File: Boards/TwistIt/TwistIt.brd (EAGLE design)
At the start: 39.9 x 54.8 mm, 19 parts

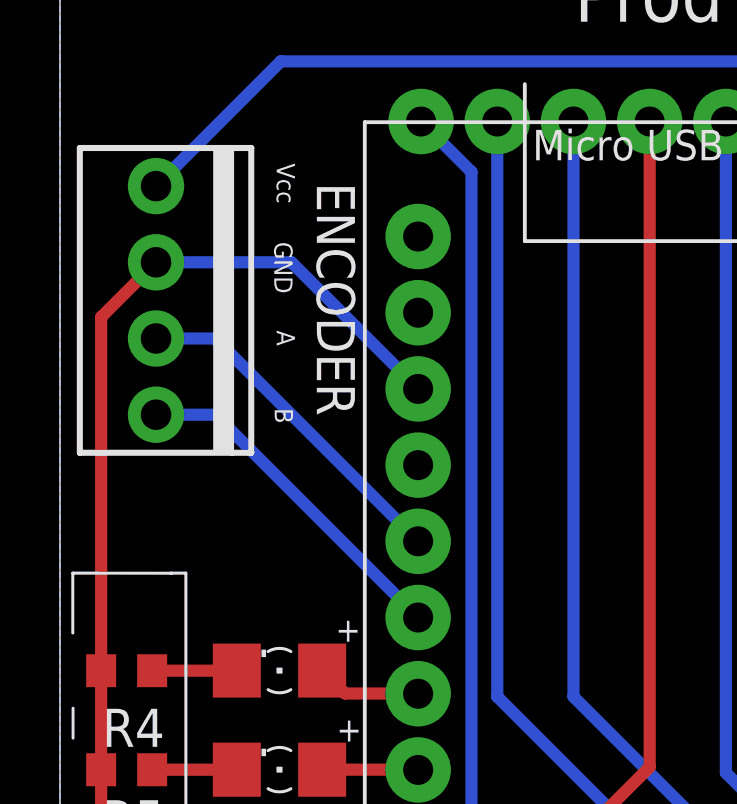
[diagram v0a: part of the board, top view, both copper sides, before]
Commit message: Add pullup resistors to encoders
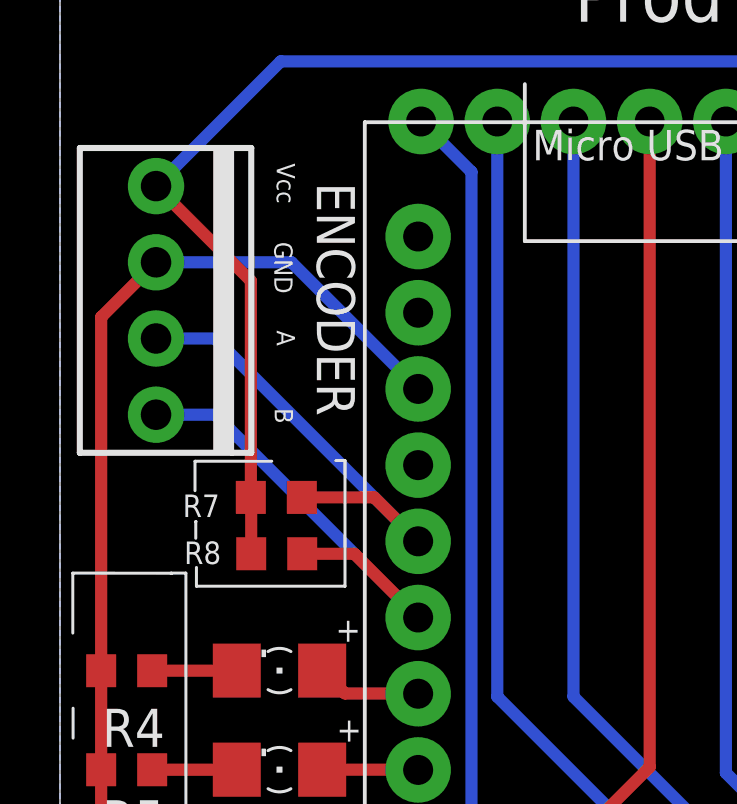
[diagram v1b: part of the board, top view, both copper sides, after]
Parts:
- added R7, R8: 10k, pie:R0603
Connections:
- net A: now also R7.1
- net B: now also R8.1
- net VCC: now also R7.2, R8.2
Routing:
- net VCC: track 74.1 -> 87.6 mm
- net B: track 11.5 -> 16.3 mm
- net A: track 11.5 -> 16.0 mm
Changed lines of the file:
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@@
 <layer number="22" name="bPlace" color="24" fill="1" visible="yes" active="yes"/>
 <layer number="23" name="tOrigins" color="15" fill="1" visible="yes" active="yes"/>
-<layer number="24" name="bOrigins" color="15" fill="1" visible="yes" active="yes"/>
+<layer number="24" name="bOrigins" color="15" fill="1" visible="no" active="yes"/>
 <layer number="25" name="tNames" color="7" fill="1" visible="yes" active="yes"/>
-<layer number="26" name="bNames" color="7" fill="1" visible="yes" active="yes"/>
+<layer number="26" name="bNames" color="7" fill="1" visible="no" active="yes"/>
 <layer number="27" name="tValues" color="7" fill="1" visible="yes" active="yes"/>
-<layer number="28" name="bValues" color="7" fill="1" visible="yes" active="yes"/>
+<layer number="28" name="bValues" color="7" fill="1" visible="no" active="yes"/>
 <layer number="29" name="tStop" color="7" fill="3" visible="yes" active="yes"/>
 <layer number="30" name="bStop" color="7" fill="6" visible="yes" active="yes"/>
@@
 <text x="10.058" y="24.313" size="0.8128" layer="25" font="vector" rot="MR0">+</text>
 <text x="10.003" y="20.986" size="0.8128" layer="25" font="vector" rot="MR0">+</text>
+<wire x1="7.059" y1="33.658" x2="4.501" y2="33.658" width="0.1" layer="21"/>
+<wire x1="4.501" y1="33.658" x2="4.501" y2="32.675" width="0.1" layer="21"/>
+<wire x1="4.536" y1="31.645" x2="4.525" y2="31.645" width="0.1" layer="21"/>
+<wire x1="4.525" y1="31.645" x2="4.525" y2="31.089" width="0.1" layer="21"/>
+<wire x1="4.548" y1="30.118" x2="4.548" y2="29.493" width="0.1" layer="21"/>
+<wire x1="4.548" y1="29.493" x2="9.5" y2="29.493" width="0.1" layer="21"/>
+<wire x1="9.5" y1="29.493" x2="9.5" y2="33.681" width="0.1" layer="21"/>
+<wire x1="9.5" y1="33.681" x2="9.188" y2="33.681" width="0.1" layer="21"/>
 </plain>
 <attributes>
@@
 <attribute name="VALUE" x="-1.244" y="44.099" size="1.27" layer="27" font="vector" rot="R270"/>
 </element>
+<element name="R7" library="pie" package="R0603" value="10k" x="7.212" y="32.452" smashed="yes" rot="R180">
+<attribute name="MANUFACTURER_PART_NUMBER" value="" x="7.212" y="32.452" size="1.778" layer="27" rot="R180" display="off"/>
+<attribute name="DISTRIBUTOR" value="DigiKey" x="7.212" y="32.452" size="1.778" layer="27" rot="R180" display="off"/>
+<attribute name="PACKAGE" value="R0603" x="7.212" y="32.452" size="1.778" layer="27" rot="R180" display="off"/>
+<attribute name="NOTES" value="Cut Tape" x="7.212" y="32.452" size="1.778" layer="27" rot="R180" display="off"/>
+<attribute name="DESCRIPTION" value="RESISTOR, American symbol" x="7.212" y="32.452" size="1.778" layer="27" rot="R180" display="off"/>
+<attribute name="MANUFACTURER" value="Rohm Semiconductor" x="7.212" y="32.452" size="1.778" layer="27" rot="R180" display="off"/>
+<attribute name="DISTRIBUTOR_PART_NUMBER" value="" x="7.212" y="32.452" size="1.778" layer="27" rot="R180" display="off"/>
+<attribute name="NAME" x="5.323" y="32.548" size="0.75" layer="25" font="vector" ratio="10" rot="R180"/>
+<attribute name="VALUE" x="9.199" y="34.125" size="0.75" layer="27" font="vector" rot="R180"/>
+</element>
+<element name="R8" library="pie" package="R0603" value="10k" x="7.224" y="30.573" smashed="yes" rot="R180">
+<attribute name="MANUFACTURER_PART_NUMBER" value="" x="7.224" y="30.573" size="1.778" layer="27" rot="R180" display="off"/>
+<attribute name="DISTRIBUTOR" value="DigiKey" x="7.224" y="30.573" size="1.778" layer="27" rot="R180" display="off"/>
+<attribute name="PACKAGE" value="R0603" x="7.224" y="30.573" size="1.778" layer="27" rot="R180" display="off"/>
+<attribute name="NOTES" value="Cut Tape" x="7.224" y="30.573" size="1.778" layer="27" rot="R180" display="off"/>
+<attribute name="DESCRIPTION" value="RESISTOR, American symbol" x="7.224" y="30.573" size="1.778" layer="27" rot="R180" display="off"/>
+<attribute name="MANUFACTURER" value="Rohm Semiconductor" x="7.224" y="30.573" size="1.778" layer="27" rot="R180" display="off"/>
+<attribute name="DISTRIBUTOR_PART_NUMBER" value="" x="7.224" y="30.573" size="1.778" layer="27" rot="R180" display="off"/>
+<attribute name="NAME" x="5.37" y="30.981" size="0.75" layer="25" font="vector" ratio="10" rot="R180"/>
+</element>
 </elements>
 <signals>
@@
 <wire x1="33.016" y1="5.512865625" x2="33.016" y2="33.278" width="0.4064" layer="16"/>
 <wire x1="33.016" y1="33.278" x2="32.766" y2="33.528" width="0.4064" layer="16"/>
+<contactref element="R8" pad="2"/>
+<contactref element="R7" pad="2"/>
+<wire x1="6.374" y1="30.573" x2="6.374" y2="32.44" width="0.4064" layer="1"/>
+<wire x1="6.374" y1="32.44" x2="6.362" y2="32.452" width="0.4064" layer="1"/>
+<wire x1="3.201" y1="42.829" x2="6.362" y2="39.668" width="0.4064" layer="1"/>
+<wire x1="6.362" y1="39.668" x2="6.362" y2="32.452" width="0.4064" layer="1"/>
 </signal>
 <signal name="P1">
@@
 <wire x1="3.201" y1="37.749" x2="5.177" y2="37.749" width="0.4064" layer="16"/>
 <wire x1="5.177" y1="37.749" x2="11.938" y2="30.988" width="0.4064" layer="16"/>
+<contactref element="R7" pad="1"/>
+<wire x1="8.062" y1="32.452" x2="10.474" y2="32.452" width="0.4064" layer="1"/>
+<wire x1="10.474" y1="32.452" x2="11.938" y2="30.988" width="0.4064" layer="1"/>
 </signal>
 <signal name="B">
@@
 <wire x1="3.201" y1="35.209" x2="5.177" y2="35.209" width="0.4064" layer="16"/>
 <wire x1="5.177" y1="35.209" x2="11.938" y2="28.448" width="0.4064" layer="16"/>
+<contactref element="R8" pad="1"/>
+<wire x1="8.074" y1="30.573" x2="9.813" y2="30.573" width="0.4064" layer="1"/>
+<wire x1="9.813" y1="30.573" x2="11.938" y2="28.448" width="0.4064" layer="1"/>
 </signal>
 </signals>

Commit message: Change pullup resistor vcalue
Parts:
- R7, R8: value 10k -> 1k
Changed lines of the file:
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@@
 <attribute name="VALUE" x="-1.244" y="44.099" size="1.27" layer="27" font="vector" rot="R270"/>
 </element>
-<element name="R7" library="pie" package="R0603" value="10k" x="7.212" y="32.452" smashed="yes" rot="R180">
+<element name="R7" library="pie" package="R0603" value="1k" x="7.212" y="32.452" smashed="yes" rot="R180">
 <attribute name="MANUFACTURER_PART_NUMBER" value="" x="7.212" y="32.452" size="1.778" layer="27" rot="R180" display="off"/>
 <attribute name="DISTRIBUTOR" value="DigiKey" x="7.212" y="32.452" size="1.778" layer="27" rot="R180" display="off"/>
@@
 <attribute name="DISTRIBUTOR_PART_NUMBER" value="" x="7.212" y="32.452" size="1.778" layer="27" rot="R180" display="off"/>
 <attribute name="NAME" x="5.323" y="32.548" size="0.75" layer="25" font="vector" ratio="10" rot="R180"/>
-<attribute name="VALUE" x="9.199" y="34.125" size="0.75" layer="27" font="vector" rot="R180"/>
+<attribute name="VALUE" x="8.817" y="34.165" size="0.75" layer="27" font="vector" rot="R180"/>
 </element>
-<element name="R8" library="pie" package="R0603" value="10k" x="7.224" y="30.573" smashed="yes" rot="R180">
+<element name="R8" library="pie" package="R0603" value="1k" x="7.224" y="30.573" smashed="yes" rot="R180">
 <attribute name="MANUFACTURER_PART_NUMBER" value="" x="7.224" y="30.573" size="1.778" layer="27" rot="R180" display="off"/>
 <attribute name="DISTRIBUTOR" value="DigiKey" x="7.224" y="30.573" size="1.778" layer="27" rot="R180" display="off"/>

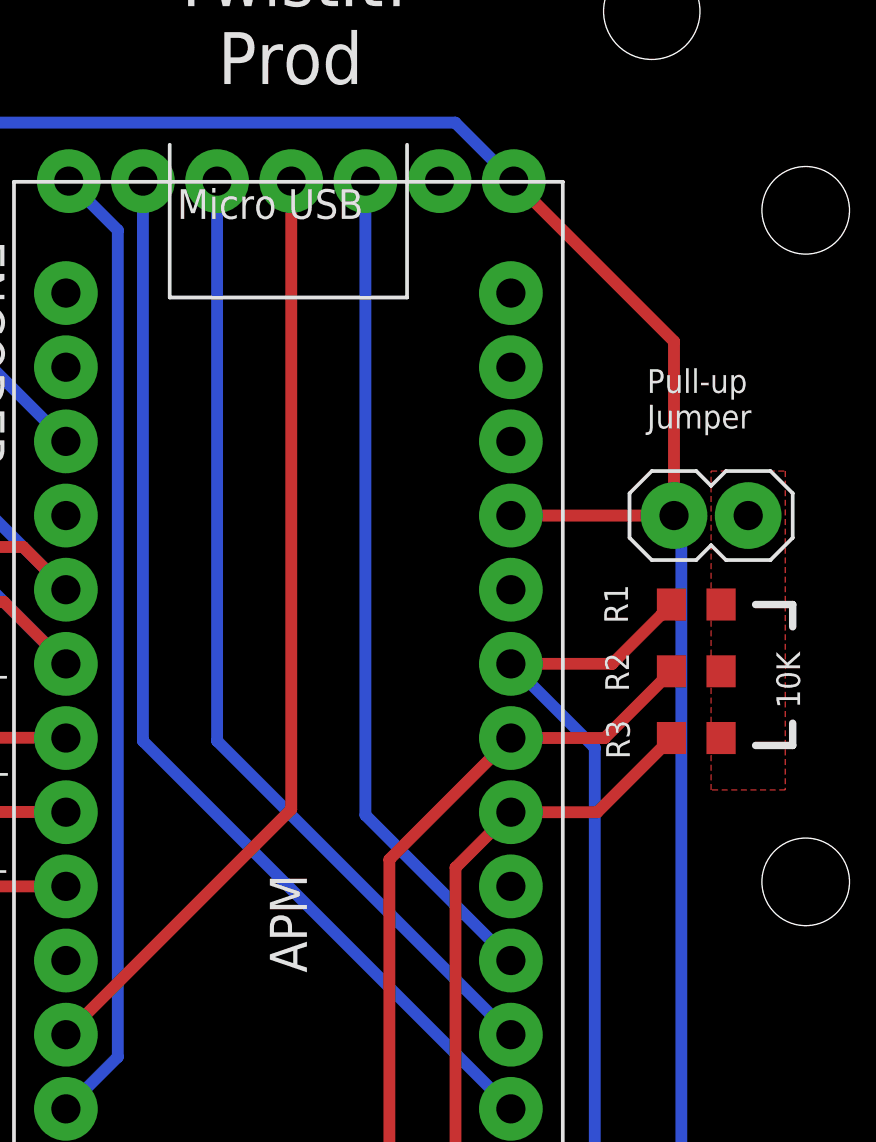
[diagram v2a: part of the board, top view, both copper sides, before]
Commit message: Rerouted EN to A3 from 14
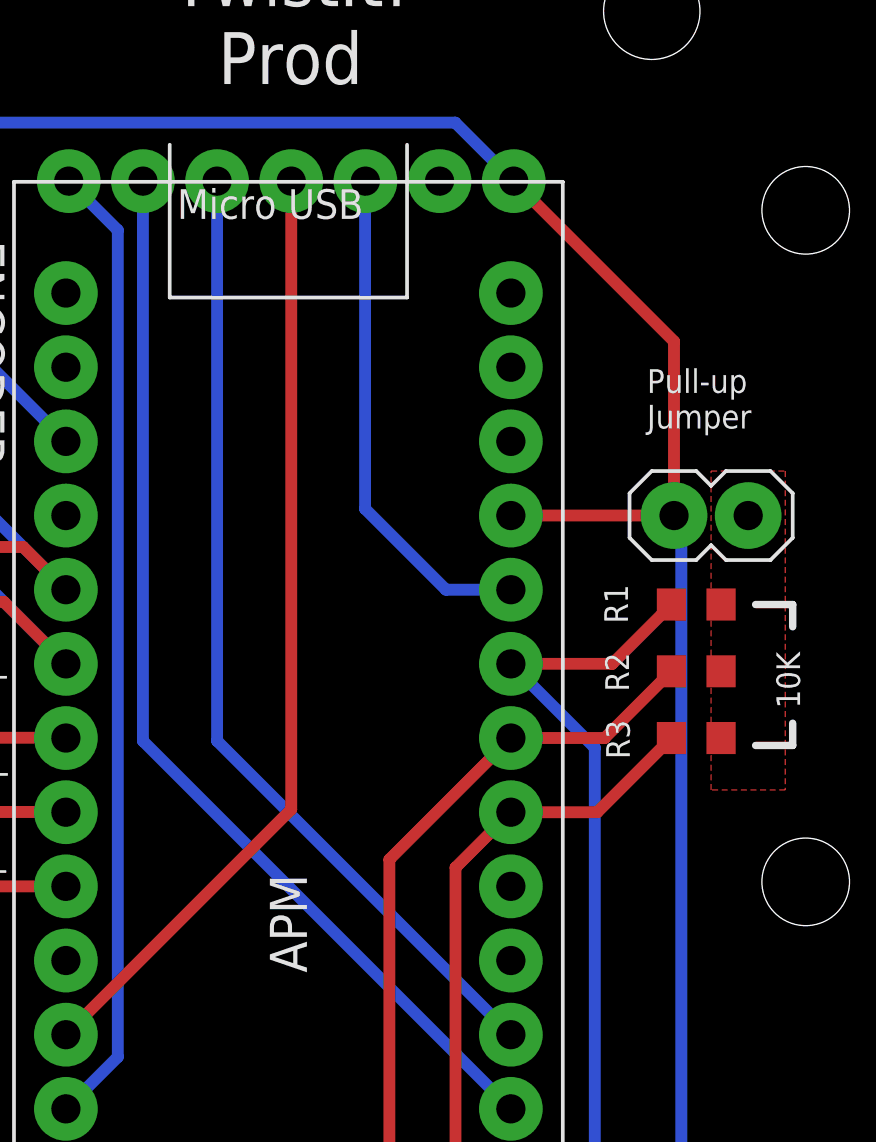
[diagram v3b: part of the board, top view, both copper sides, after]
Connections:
- net EN: now also APM.A3; no longer APM.14
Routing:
- net EN: track 28.8 -> 17.4 mm
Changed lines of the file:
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@@
 <?xml version="1.0" encoding="utf-8"?>
 <!DOCTYPE eagle SYSTEM "eagle.dtd">
-<eagle version="7.6.0">
+<eagle version="6.6.0">
 <drawing>
 <settings>
@@
 <pass name="Default">
 <param name="RoutingGrid" value="50mil"/>
-<param name="AutoGrid" value="1"/>
-<param name="Efforts" value="0"/>
-<param name="TopRouterVariant" value="1"/>
 <param name="tpViaShape" value="round"/>
-<param name="PrefDir.1" value="a"/>
+<param name="PrefDir.1" value="|"/>
 <param name="PrefDir.2" value="0"/>
 <param name="PrefDir.3" value="0"/>
@@
 <param name="PrefDir.14" value="0"/>
 <param name="PrefDir.15" value="0"/>
-<param name="PrefDir.16" value="a"/>
+<param name="PrefDir.16" value="-"/>
 <param name="cfVia" value="8"/>
 <param name="cfNonPref" value="5"/>
@@
 <signal name="EN">
 <contactref element="BR1" pad="EN"/>
-<contactref element="APM" pad="14"/>
-<wire x1="22.196" y1="44.982" x2="22.196" y2="23.27" width="0.4064" layer="16"/>
-<wire x1="22.196" y1="23.27" x2="27.178" y2="18.288" width="0.4064" layer="16"/>
+<contactref element="APM" pad="A3"/>
+<wire x1="27.178" y1="30.988" x2="24.955" y2="30.988" width="0.4064" layer="16"/>
+<wire x1="24.955" y1="30.988" x2="22.184" y2="33.759" width="0.4064" layer="16"/>
+<wire x1="22.184" y1="33.759" x2="22.184" y2="44.97" width="0.4064" layer="16"/>
+<wire x1="22.184" y1="44.97" x2="22.196" y2="44.982" width="0.4064" layer="16"/>
 </signal>
 <signal name="CS">

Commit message: cronCH
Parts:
- moved BR1 63.3 mm to (45.1, 24.4), flipped to the top, turned to 0 degrees
- moved R3 6.20 mm to (31.3, 20.1), turned to 90 degrees
- moved R2 3.80 mm to (31.4, 25.1), turned to 90 degrees
- moved R1 3.64 mm to (30.5, 28.5), turned to 90 degrees
- moved 5V_JUMPER 3.21 mm to (30.8, 33.6), turned to 270 degrees
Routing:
- net CS: track 32.4 -> 10.9 mm
- net INB: track 37.0 -> 17.8 mm
- net INA: track 33.4 -> 14.2 mm
- net 5V: track 0.00 -> 13.7 mm
- net VCC: track 87.6 -> 78.4 mm
- net P1: track 31.3 -> 28.6 mm
- net PWM: track 33.2 -> 30.8 mm
- net P2: track 28.6 -> 27.0 mm
- net P3: track 35.4 -> 34.6 mm
- removed copper zone on layer 1, net 5V
